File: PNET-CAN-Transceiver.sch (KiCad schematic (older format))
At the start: 15 parts

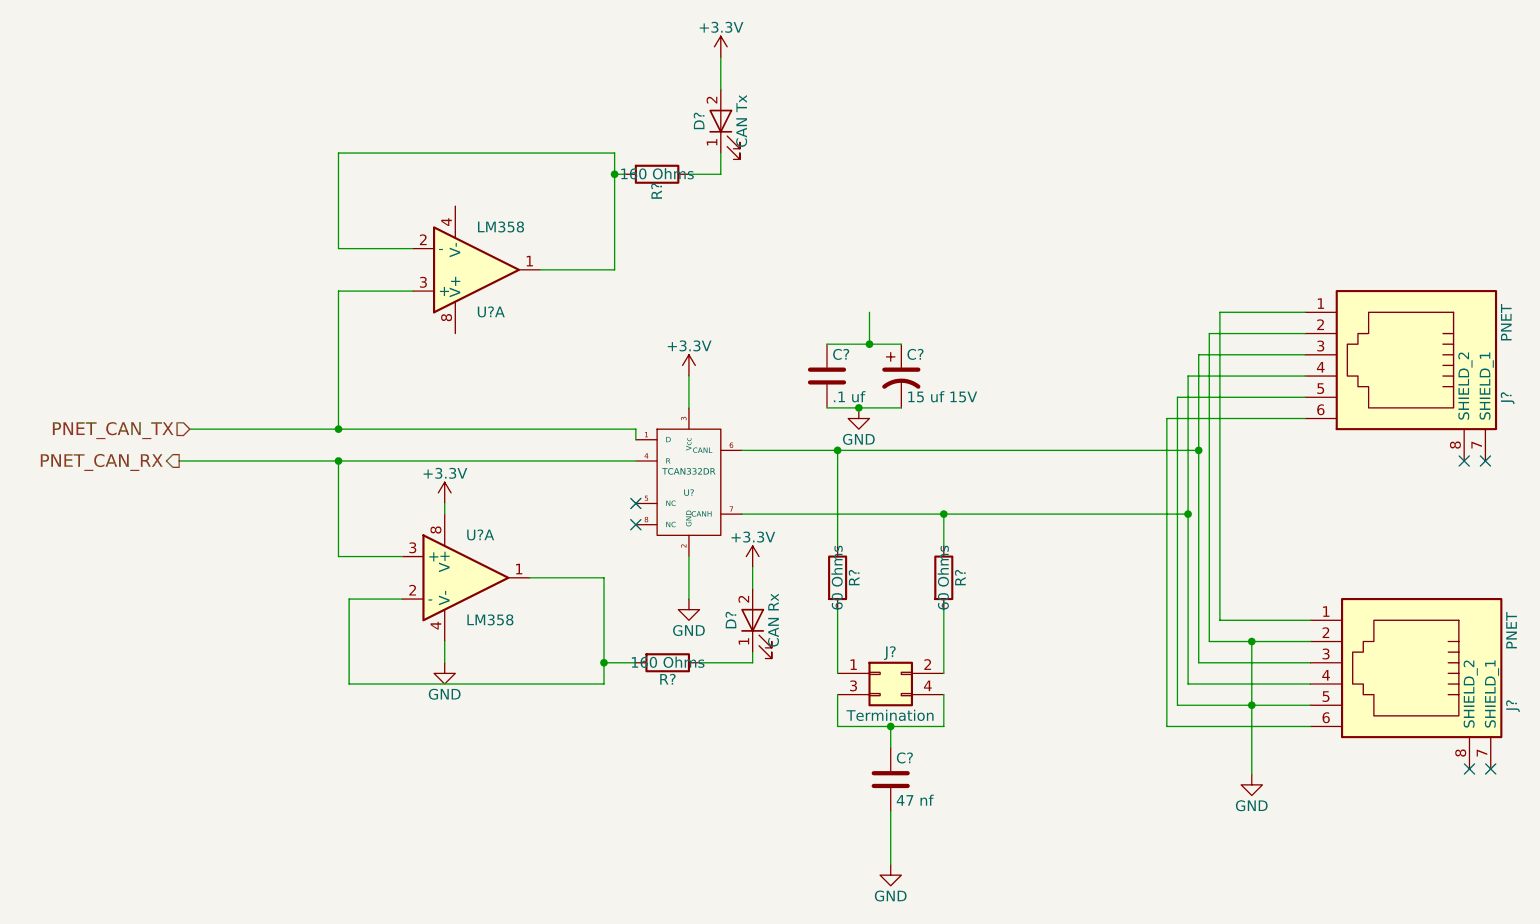
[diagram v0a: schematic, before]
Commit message: Start on LCC <=> PNET router.
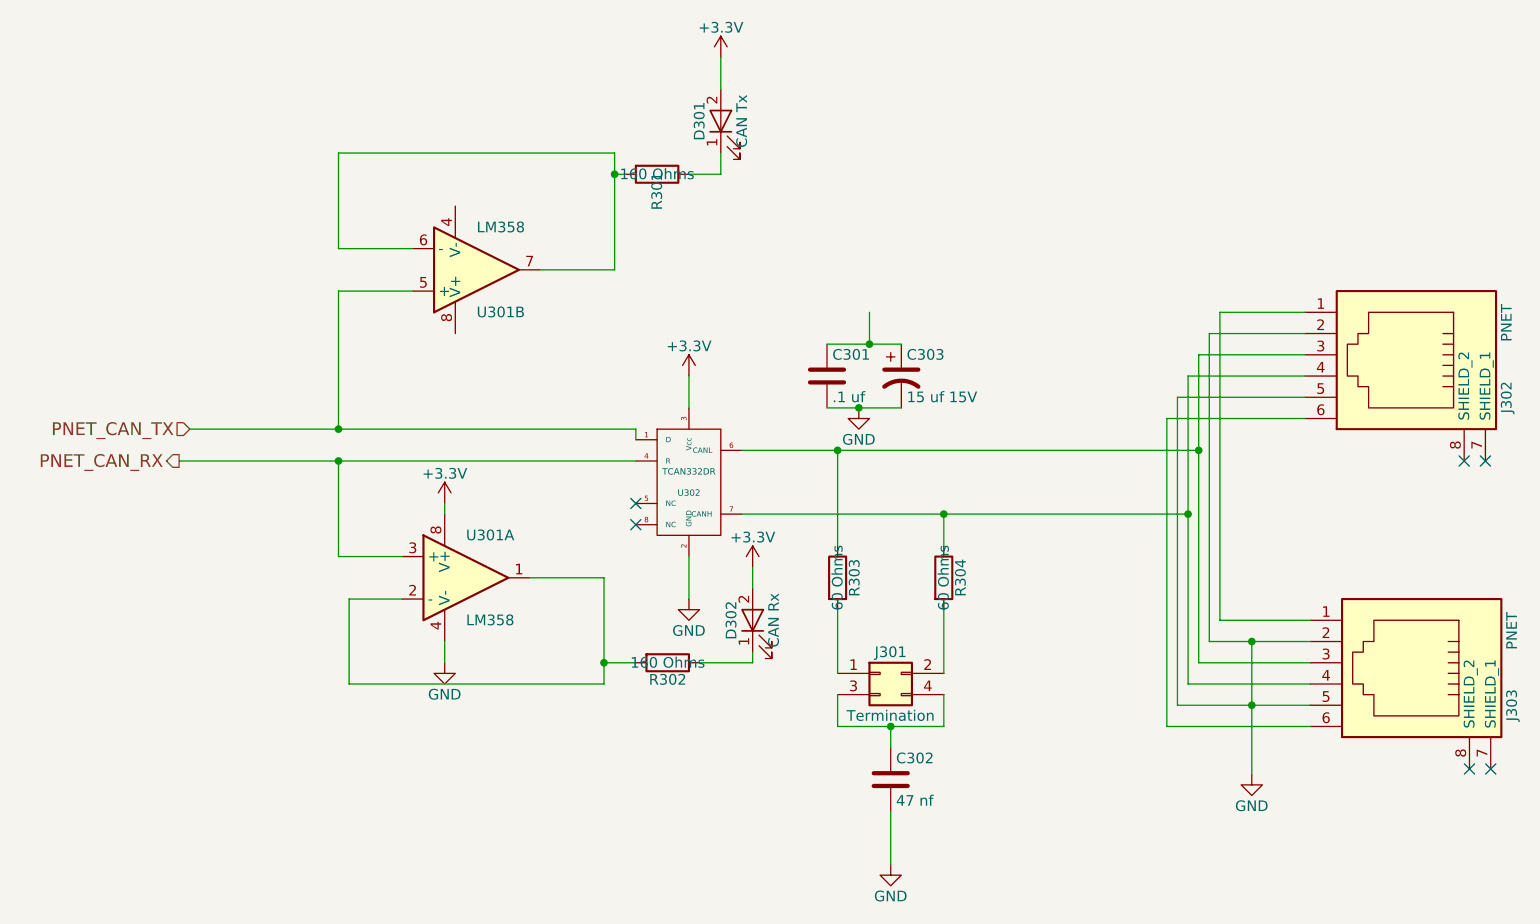
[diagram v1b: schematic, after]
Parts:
- gave numbers to parts that had none: 14
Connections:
- net PNET_CAN_TX: now also U301.5 (+); no longer U301.3 (+)
- new net: R301.2, U301.6 (-), U301.7
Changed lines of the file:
@@
 $EndDescr
 $Comp
-L TCAN332DR U?
+L TCAN332DR U302
 U 1 1 63C03DBA
 P 4600 2950
-F 0 "U?" H 4600 2900 30  0000 C CNN
+F 0 "U302" H 4600 2900 30  0000 C CNN
 F 1 "TCAN332DR" H 4600 3000 30  0000 C CNN
 F 2 "Housings_SOIC:SOIC-8-1EP_3.9x4.9mm_Pitch1.27mm" H 4600 2950 60  0001 C CNN
@@
 NoConn ~ 4350 3150
 $Comp
-L +3.3V #PWR?
+L +3.3V #PWR019
 U 1 1 63C03DBD
 P 4600 2450
-F 0 "#PWR?" H 4600 2300 50  0001 C CNN
+F 0 "#PWR019" H 4600 2300 50  0001 C CNN
 F 1 "+3.3V" H 4600 2590 50  0000 C CNN
 F 2 "" H 4600 2450 50  0001 C CNN
@@
 $EndComp
 $Comp
-L GND #PWR?
+L GND #PWR020
 U 1 1 63C03DBE
 P 4600 3500
-F 0 "#PWR?" H 4600 3250 50  0001 C CNN
+F 0 "#PWR020" H 4600 3250 50  0001 C CNN
 F 1 "GND" H 4600 3350 50  0000 C CNN
 F 2 "" H 4600 3500 50  0001 C CNN
@@
 $EndComp
 $Comp
-L C C?
+L C C301
 U 1 1 63C03DC0
 P 5250 2450
-F 0 "C?" H 5275 2550 50  0000 L CNN
+F 0 "C301" H 5275 2550 50  0000 L CNN
 F 1 ".1 uf" H 5275 2350 50  0000 L CNN
 F 2 "Capacitors_THT:C_Rect_L4.0mm_W2.5mm_P2.50mm" H 5288 2300 50  0001 C CNN
@@
 $EndComp
 $Comp
-L CP1 C?
+L CP1 C303
 U 1 1 63C03DC1
 P 5600 2450
-F 0 "C?" H 5625 2550 50  0000 L CNN
+F 0 "C303" H 5625 2550 50  0000 L CNN
 F 1 "15 uf 15V" H 5625 2350 50  0000 L CNN
 F 2 "Capacitors_THT:CP_Radial_D6.3mm_P2.50mm" H 5600 2450 50  0001 C CNN
@@
 $EndComp
 $Comp
-L Conn_02x02_Odd_Even J?
+L Conn_02x02_Odd_Even J301
 U 1 1 63C03DC2
 P 5500 3850
-F 0 "J?" H 5550 3950 50  0000 C CNN
+F 0 "J301" H 5550 3950 50  0000 C CNN
 F 1 "Termination" H 5550 3650 50  0000 C CNN
 F 2 "Pin_Headers:Pin_Header_Straight_2x02_Pitch2.54mm" H 5500 3850 50  0001 C CNN
@@
 $EndComp
 $Comp
-L R R?
+L R R303
 U 1 1 63C03DC3
 P 5300 3400
-F 0 "R?" V 5380 3400 50  0000 C CNN
+F 0 "R303" V 5380 3400 50  0000 C CNN
 F 1 "60 Ohms" V 5300 3400 50  0000 C CNN
 F 2 "Resistors_THT:R_Axial_DIN0204_L3.6mm_D1.6mm_P2.54mm_Vertical" V 5230 3400 50  0001 C CNN
@@
 $EndComp
 $Comp
-L R R?
+L R R304
 U 1 1 63C03DC4
 P 5800 3400
-F 0 "R?" V 5880 3400 50  0000 C CNN
+F 0 "R304" V 5880 3400 50  0000 C CNN
 F 1 "60 Ohms" V 5800 3400 50  0000 C CNN
 F 2 "Resistors_THT:R_Axial_DIN0204_L3.6mm_D1.6mm_P2.54mm_Vertical" V 5730 3400 50  0001 C CNN
@@
 $EndComp
 $Comp
-L C C?
+L C C302
 U 1 1 63C03DC5
 P 5550 4350
-F 0 "C?" H 5575 4450 50  0000 L CNN
+F 0 "C302" H 5575 4450 50  0000 L CNN
 F 1 "47 nf" H 5575 4250 50  0000 L CNN
 F 2 "Capacitors_THT:C_Rect_L4.0mm_W2.5mm_P2.50mm" H 5588 4200 50  0001 C CNN
@@
 $EndComp
 $Comp
-L GND #PWR?
+L GND #PWR021
 U 1 1 63C03DC6
 P 5550 4750
-F 0 "#PWR?" H 5550 4500 50  0001 C CNN
+F 0 "#PWR021" H 5550 4500 50  0001 C CNN
 F 1 "GND" H 5550 4600 50  0000 C CNN
 F 2 "" H 5550 4750 50  0001 C CNN
@@
 $EndComp
 $Comp
-L GND #PWR?
+L GND #PWR022
 U 1 1 63C03DC8
 P 5400 2600
-F 0 "#PWR?" H 5400 2350 50  0001 C CNN
+F 0 "#PWR022" H 5400 2350 50  0001 C CNN
 F 1 "GND" H 5400 2450 50  0000 C CNN
 F 2 "" H 5400 2600 50  0001 C CNN
@@
 PNET_CAN_RX
 $Comp
-L LM358 U?
-U 1 1 63C03DCE
+L LM358 U301
+U 2 1 63C03DCE
 P 3600 1950
-F 0 "U?" H 3600 2150 50  0000 L CNN
+F 0 "U301" H 3600 2150 50  0000 L CNN
 F 1 "LM358" H 3600 1750 50  0000 L CNN
 F 2 "Housings_DIP:DIP-8_W7.62mm" H 3600 1950 50  0001 C CNN
 F 3 "" H 3600 1950 50  0001 C CNN
 F 4 "595-LM358AP" H 3600 1950 60  0001 C CNN "Mouser Part Number"
-	1    3600 1950
+	2    3600 1950
 	1    0    0    1
 $EndComp
 $Comp
-L LM358 U?
+L LM358 U301
 U 1 1 63C03DCF
 P 3550 3400
-F 0 "U?" H 3550 3600 50  0000 L CNN
+F 0 "U301" H 3550 3600 50  0000 L CNN
 F 1 "LM358" H 3550 3200 50  0000 L CNN
 F 2 "Housings_DIP:DIP-8_W7.62mm" H 3550 3400 50  0001 C CNN
@@
 $EndComp
 $Comp
-L GND #PWR?
+L GND #PWR023
 U 1 1 63C03DD0
 P 3450 3800
-F 0 "#PWR?" H 3450 3550 50  0001 C CNN
+F 0 "#PWR023" H 3450 3550 50  0001 C CNN
 F 1 "GND" H 3450 3650 50  0000 C CNN
 F 2 "" H 3450 3800 50  0001 C CNN
@@
 $EndComp
 $Comp
-L +3.3V #PWR?
+L +3.3V #PWR024
 U 1 1 63C03DD1
 P 3450 3050
-F 0 "#PWR?" H 3450 2900 50  0001 C CNN
+F 0 "#PWR024" H 3450 2900 50  0001 C CNN
 F 1 "+3.3V" H 3450 3190 50  0000 C CNN
 F 2 "" H 3450 3050 50  0001 C CNN
@@
 $EndComp
 $Comp
-L R R?
+L R R301
 U 1 1 63C03DD2
 P 4450 1500
-F 0 "R?" H 4530 1500 50  0000 C CNN
+F 0 "R301" H 4530 1500 50  0000 C CNN
 F 1 "160 Ohms" V 4450 1500 50  0000 C CNN
 F 2 "Resistors_THT:R_Axial_DIN0204_L3.6mm_D1.6mm_P1.90mm_Vertical" V 4380 1500 50  0001 C CNN
@@
 $EndComp
 $Comp
-L R R?
+L R R302
 U 1 1 63C03DD3
 P 4500 3800
-F 0 "R?" V 4580 3800 50  0000 C CNN
+F 0 "R302" V 4580 3800 50  0000 C CNN
 F 1 "160 Ohms" V 4500 3800 50  0000 C CNN
 F 2 "Resistors_THT:R_Axial_DIN0204_L3.6mm_D1.6mm_P1.90mm_Vertical" V 4430 3800 50  0001 C CNN
@@
 $EndComp
 $Comp
-L LED D?
+L LED D301
 U 1 1 63C03DD4
 P 4750 1250
-F 0 "D?" H 4750 1350 50  0000 C CNN
+F 0 "D301" H 4750 1350 50  0000 C CNN
 F 1 "CAN Tx" H 4750 1150 50  0000 C CNN
 F 2 "LEDs:LED_D3.0mm" H 4750 1250 50  0001 C CNN
@@
 $EndComp
 $Comp
-L LED D?
+L LED D302
 U 1 1 63C03DD5
 P 4900 3600
-F 0 "D?" H 4900 3700 50  0000 C CNN
+F 0 "D302" H 4900 3700 50  0000 C CNN
 F 1 "CAN Rx" H 4900 3500 50  0000 C CNN
 F 2 "LEDs:LED_D3.0mm" H 4900 3600 50  0001 C CNN
@@
 $EndComp
 $Comp
-L +3.3V #PWR?
+L +3.3V #PWR025
 U 1 1 63C03DD6
 P 4750 950
-F 0 "#PWR?" H 4750 800 50  0001 C CNN
+F 0 "#PWR025" H 4750 800 50  0001 C CNN
 F 1 "+3.3V" H 4750 1090 50  0000 C CNN
 F 2 "" H 4750 950 50  0001 C CNN
@@
 $EndComp
 $Comp
-L +3.3V #PWR?
+L +3.3V #PWR026
 U 1 1 63C03DD7
 P 4900 3350
-F 0 "#PWR?" H 4900 3200 50  0001 C CNN
+F 0 "#PWR026" H 4900 3200 50  0001 C CNN
 F 1 "+3.3V" H 4900 3490 50  0000 C CNN
 F 2 "" H 4900 3350 50  0001 C CNN
@@
 $EndComp
 $Comp
-L RJ12 J?
+L RJ12 J302
 U 1 1 63C04A35
 P 7950 2350
-F 0 "J?" H 8150 2850 50  0000 C CNN
+F 0 "J302" H 8150 2850 50  0000 C CNN
 F 1 "PNET" H 7800 2850 50  0000 C CNN
 F 2 "Connectors:RJ12_E" H 7950 2350 50  0001 C CNN
@@
 $EndComp
 $Comp
-L RJ12 J?
+L RJ12 J303
 U 1 1 63C04C52
 P 7975 3800
-F 0 "J?" H 8175 4300 50  0000 C CNN
+F 0 "J303" H 8175 4300 50  0000 C CNN
 F 1 "PNET" H 7825 4300 50  0000 C CNN
 F 2 "Connectors:RJ12_E" H 7975 3800 50  0001 C CNN
@@
 $EndComp
 $Comp
-L GND #PWR?
+L GND #PWR027
 U 1 1 63C05BB2
 P 7250 4325
-F 0 "#PWR?" H 7250 4075 50  0001 C CNN
+F 0 "#PWR027" H 7250 4075 50  0001 C CNN
 F 1 "GND" H 7250 4175 50  0000 C CNN
 F 2 "" H 7250 4325 50  0001 C CNN

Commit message: Completed initial HW design.
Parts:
- C301: footprint Capacitors_THT:C_Rect_L4.0mm_W2.5mm_P2.50mm -> Capacitors_SMD:C_0603; Mouser Part Number 594-K104Z15Y5VF5TL2 -> 603-CC603KPX7R9BB104
- C302: footprint Capacitors_THT:C_Rect_L4.0mm_W2.5mm_P2.50mm -> Capacitors_SMD:C_0603; Mouser Part Number 594-K473K15X7RF5TL2 -> 963-GMK107BJ473KAHT
- C303: footprint Capacitors_THT:CP_Radial_D6.3mm_P2.50mm -> Capacitors_SMD:CP_Elec_4x5.8; Mouser Part Number 710-860080773002 -> 647-UUD1C150MCL
- D301: value CAN Tx -> PNET Tx; footprint LEDs:LED_D3.0mm -> LEDs:LED_0603; Mouser Part Number 710-151031SS04000 -> 710-150060SS75000
- D302: value CAN Rx -> PNET Rx; footprint LEDs:LED_D3.0mm -> LEDs:LED_0603; Mouser Part Number 710-151033YS03000 -> 710-150060YS75000
- R301, R302: footprint Resistors_THT:R_Axial_DIN0204_L3.6mm_D1.6mm_P1.90mm_Vertical -> Resistors_SMD:R_0603; Mouser Part Number 603-CFR-25JB-52-160R -> 603-AC0603JR-07160RL
- R303, R304: footprint Resistors_THT:R_Axial_DIN0204_L3.6mm_D1.6mm_P2.54mm_Vertical -> Resistors_SMD:R_1206; Mouser Part Number 603-RSF2WSJT-52-60R -> 71-CRCW120660R0KNAIF
- U301: footprint Housings_DIP:DIP-8_W7.62mm -> Housings_SOIC:SOIC-8_3.9x4.9mm_Pitch1.27mm; Mouser Part Number 595-LM358AP -> 595-LM358DR
- U302: footprint Housings_SOIC:SOIC-8-1EP_3.9x4.9mm_Pitch1.27mm -> Housings_SOIC:SOIC-8_3.9x4.9mm_Pitch1.27mm
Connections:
- net +3V3: now also C301.1, C303.1
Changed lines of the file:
@@
 LIBS:lm2574n-5
 LIBS:sn65hvd233-ht
+LIBS:ap63205
 LIBS:LCC-PNET-Router-cache
 EELAYER 25 0
@@
 F 0 "U302" H 4600 2900 30  0000 C CNN
 F 1 "TCAN332DR" H 4600 3000 30  0000 C CNN
-F 2 "Housings_SOIC:SOIC-8-1EP_3.9x4.9mm_Pitch1.27mm" H 4600 2950 60  0001 C CNN
+F 2 "Housings_SOIC:SOIC-8_3.9x4.9mm_Pitch1.27mm" H 4600 2950 60  0001 C CNN
 F 3 "" H 4600 2950 60  0000 C CNN
 F 4 "595-TCAN332DR" H 4600 2950 60  0001 C CNN "Mouser Part Number"
@@
 NoConn ~ 4350 3150
 $Comp
-L +3.3V #PWR019
+L +3.3V #PWR303
 U 1 1 63C03DBD
 P 4600 2450
-F 0 "#PWR019" H 4600 2300 50  0001 C CNN
+F 0 "#PWR303" H 4600 2300 50  0001 C CNN
 F 1 "+3.3V" H 4600 2590 50  0000 C CNN
 F 2 "" H 4600 2450 50  0001 C CNN
@@
 $EndComp
 $Comp
-L GND #PWR020
+L GND #PWR304
 U 1 1 63C03DBE
 P 4600 3500
-F 0 "#PWR020" H 4600 3250 50  0001 C CNN
+F 0 "#PWR304" H 4600 3250 50  0001 C CNN
 F 1 "GND" H 4600 3350 50  0000 C CNN
 F 2 "" H 4600 3500 50  0001 C CNN
@@
 F 0 "C301" H 5275 2550 50  0000 L CNN
 F 1 ".1 uf" H 5275 2350 50  0000 L CNN
-F 2 "Capacitors_THT:C_Rect_L4.0mm_W2.5mm_P2.50mm" H 5288 2300 50  0001 C CNN
+F 2 "Capacitors_SMD:C_0603" H 5288 2300 50  0001 C CNN
 F 3 "" H 5250 2450 50  0001 C CNN
-F 4 "594-K104Z15Y5VF5TL2" H 5250 2450 60  0001 C CNN "Mouser Part Number"
+F 4 "603-CC603KPX7R9BB104" H 5250 2450 60  0001 C CNN "Mouser Part Number"
 	1    5250 2450
 	1    0    0    -1
@@
 F 0 "C303" H 5625 2550 50  0000 L CNN
 F 1 "15 uf 15V" H 5625 2350 50  0000 L CNN
-F 2 "Capacitors_THT:CP_Radial_D6.3mm_P2.50mm" H 5600 2450 50  0001 C CNN
+F 2 "Capacitors_SMD:CP_Elec_4x5.8" H 5600 2450 50  0001 C CNN
 F 3 "" H 5600 2450 50  0001 C CNN
-F 4 "710-860080773002" H 5600 2450 60  0001 C CNN "Mouser Part Number"
+F 4 "647-UUD1C150MCL" H 5600 2450 60  0001 C CNN "Mouser Part Number"
 	1    5600 2450
 	1    0    0    -1
@@
 F 0 "R303" V 5380 3400 50  0000 C CNN
 F 1 "60 Ohms" V 5300 3400 50  0000 C CNN
-F 2 "Resistors_THT:R_Axial_DIN0204_L3.6mm_D1.6mm_P2.54mm_Vertical" V 5230 3400 50  0001 C CNN
+F 2 "Resistors_SMD:R_1206" V 5230 3400 50  0001 C CNN
 F 3 "" H 5300 3400 50  0001 C CNN
-F 4 "603-RSF2WSJT-52-60R" V 5300 3400 60  0001 C CNN "Mouser Part Number"
+F 4 "71-CRCW120660R0KNAIF" V 5300 3400 60  0001 C CNN "Mouser Part Number"
 	1    5300 3400
 	1    0    0    -1
@@
 F 0 "R304" V 5880 3400 50  0000 C CNN
 F 1 "60 Ohms" V 5800 3400 50  0000 C CNN
-F 2 "Resistors_THT:R_Axial_DIN0204_L3.6mm_D1.6mm_P2.54mm_Vertical" V 5730 3400 50  0001 C CNN
+F 2 "Resistors_SMD:R_1206" V 5730 3400 50  0001 C CNN
 F 3 "" H 5800 3400 50  0001 C CNN
-F 4 "603-RSF2WSJT-52-60R" V 5800 3400 60  0001 C CNN "Mouser Part Number"
+F 4 "71-CRCW120660R0KNAIF" V 5800 3400 60  0001 C CNN "Mouser Part Number"
 	1    5800 3400
 	1    0    0    -1
@@
 F 0 "C302" H 5575 4450 50  0000 L CNN
 F 1 "47 nf" H 5575 4250 50  0000 L CNN
-F 2 "Capacitors_THT:C_Rect_L4.0mm_W2.5mm_P2.50mm" H 5588 4200 50  0001 C CNN
+F 2 "Capacitors_SMD:C_0603" H 5588 4200 50  0001 C CNN
 F 3 "" H 5550 4350 50  0001 C CNN
-F 4 "594-K473K15X7RF5TL2" H 5550 4350 60  0001 C CNN "Mouser Part Number"
+F 4 "963-GMK107BJ473KAHT" H 5550 4350 60  0001 C CNN "Mouser Part Number"
 	1    5550 4350
 	1    0    0    -1
 $EndComp
 $Comp
-L GND #PWR021
+L GND #PWR309
 U 1 1 63C03DC6
 P 5550 4750
-F 0 "#PWR021" H 5550 4500 50  0001 C CNN
+F 0 "#PWR309" H 5550 4500 50  0001 C CNN
 F 1 "GND" H 5550 4600 50  0000 C CNN
 F 2 "" H 5550 4750 50  0001 C CNN
@@
 $EndComp
 $Comp
-L GND #PWR022
+L GND #PWR307
 U 1 1 63C03DC8
 P 5400 2600
-F 0 "#PWR022" H 5400 2350 50  0001 C CNN
+F 0 "#PWR307" H 5400 2350 50  0001 C CNN
 F 1 "GND" H 5400 2450 50  0000 C CNN
 F 2 "" H 5400 2600 50  0001 C CNN
@@
 F 0 "U301" H 3600 2150 50  0000 L CNN
 F 1 "LM358" H 3600 1750 50  0000 L CNN
-F 2 "Housings_DIP:DIP-8_W7.62mm" H 3600 1950 50  0001 C CNN
+F 2 "Housings_SOIC:SOIC-8_3.9x4.9mm_Pitch1.27mm" H 3600 1950 50  0001 C CNN
 F 3 "" H 3600 1950 50  0001 C CNN
-F 4 "595-LM358AP" H 3600 1950 60  0001 C CNN "Mouser Part Number"
+F 4 "595-LM358DR" H 3600 1950 60  0001 C CNN "Mouser Part Number"
 	2    3600 1950
 	1    0    0    1
@@
 F 0 "U301" H 3550 3600 50  0000 L CNN
 F 1 "LM358" H 3550 3200 50  0000 L CNN
-F 2 "Housings_DIP:DIP-8_W7.62mm" H 3550 3400 50  0001 C CNN
+F 2 "Housings_SOIC:SOIC-8_3.9x4.9mm_Pitch1.27mm" H 3550 3400 50  0001 C CNN
 F 3 "" H 3550 3400 50  0001 C CNN
-F 4 "595-LM358AP" H 3550 3400 60  0001 C CNN "Mouser Part Number"
+F 4 "595-LM358DR" H 3550 3400 60  0001 C CNN "Mouser Part Number"
 	1    3550 3400
 	1    0    0    -1
 $EndComp
 $Comp
-L GND #PWR023
+L GND #PWR302
 U 1 1 63C03DD0
 P 3450 3800
-F 0 "#PWR023" H 3450 3550 50  0001 C CNN
+F 0 "#PWR302" H 3450 3550 50  0001 C CNN
 F 1 "GND" H 3450 3650 50  0000 C CNN
 F 2 "" H 3450 3800 50  0001 C CNN
@@
 $EndComp
 $Comp
-L +3.3V #PWR024
+L +3.3V #PWR301
 U 1 1 63C03DD1
 P 3450 3050
-F 0 "#PWR024" H 3450 2900 50  0001 C CNN
+F 0 "#PWR301" H 3450 2900 50  0001 C CNN
 F 1 "+3.3V" H 3450 3190 50  0000 C CNN
 F 2 "" H 3450 3050 50  0001 C CNN
@@
 F 0 "R301" H 4530 1500 50  0000 C CNN
 F 1 "160 Ohms" V 4450 1500 50  0000 C CNN
-F 2 "Resistors_THT:R_Axial_DIN0204_L3.6mm_D1.6mm_P1.90mm_Vertical" V 4380 1500 50  0001 C CNN
+F 2 "Resistors_SMD:R_0603" V 4380 1500 50  0001 C CNN
 F 3 "" H 4450 1500 50  0001 C CNN
-F 4 "603-CFR-25JB-52-160R" H 4450 1500 60  0001 C CNN "Mouser Part Number"
+F 4 "603-AC0603JR-07160RL" H 4450 1500 60  0001 C CNN "Mouser Part Number"
 	1    4450 1500
 	0    1    1    0
@@
 F 0 "R302" V 4580 3800 50  0000 C CNN
 F 1 "160 Ohms" V 4500 3800 50  0000 C CNN
-F 2 "Resistors_THT:R_Axial_DIN0204_L3.6mm_D1.6mm_P1.90mm_Vertical" V 4430 3800 50  0001 C CNN
+F 2 "Resistors_SMD:R_0603" V 4430 3800 50  0001 C CNN
 F 3 "" H 4500 3800 50  0001 C CNN
-F 4 "603-CFR-25JB-52-160R" V 4500 3800 60  0001 C CNN "Mouser Part Number"
+F 4 "603-AC0603JR-07160RL" V 4500 3800 60  0001 C CNN "Mouser Part Number"
 	1    4500 3800
 	0    1    1    0
@@
 P 4750 1250
 F 0 "D301" H 4750 1350 50  0000 C CNN
-F 1 "CAN Tx" H 4750 1150 50  0000 C CNN
-F 2 "LEDs:LED_D3.0mm" H 4750 1250 50  0001 C CNN
+F 1 "PNET Tx" H 4750 1150 50  0000 C CNN
+F 2 "LEDs:LED_0603" H 4750 1250 50  0001 C CNN
 F 3 "" H 4750 1250 50  0001 C CNN
-F 4 "710-151031SS04000" H 4750 1250 60  0001 C CNN "Mouser Part Number"
+F 4 "710-150060SS75000" H 4750 1250 60  0001 C CNN "Mouser Part Number"
 	1    4750 1250
 	0    -1   -1   0
@@
 P 4900 3600
 F 0 "D302" H 4900 3700 50  0000 C CNN
-F 1 "CAN Rx" H 4900 3500 50  0000 C CNN
-F 2 "LEDs:LED_D3.0mm" H 4900 3600 50  0001 C CNN
+F 1 "PNET Rx" H 4900 3500 50  0000 C CNN
+F 2 "LEDs:LED_0603" H 4900 3600 50  0001 C CNN
 F 3 "" H 4900 3600 50  0001 C CNN
-F 4 "710-151033YS03000" H 4900 3600 60  0001 C CNN "Mouser Part Number"
+F 4 "710-150060YS75000" H 4900 3600 60  0001 C CNN "Mouser Part Number"
 	1    4900 3600
 	0    -1   -1   0
 $EndComp
 $Comp
-L +3.3V #PWR025
+L +3.3V #PWR305
 U 1 1 63C03DD6
 P 4750 950
-F 0 "#PWR025" H 4750 800 50  0001 C CNN
+F 0 "#PWR305" H 4750 800 50  0001 C CNN
 F 1 "+3.3V" H 4750 1090 50  0000 C CNN
 F 2 "" H 4750 950 50  0001 C CNN
@@
 $EndComp
 $Comp
-L +3.3V #PWR026
+L +3.3V #PWR306
 U 1 1 63C03DD7
 P 4900 3350
-F 0 "#PWR026" H 4900 3200 50  0001 C CNN
+F 0 "#PWR306" H 4900 3200 50  0001 C CNN
 F 1 "+3.3V" H 4900 3490 50  0000 C CNN
 F 2 "" H 4900 3350 50  0001 C CNN
@@
 $EndComp
 $Comp
-L GND #PWR027
+L GND #PWR310
 U 1 1 63C05BB2
 P 7250 4325
-F 0 "#PWR027" H 7250 4075 50  0001 C CNN
+F 0 "#PWR310" H 7250 4075 50  0001 C CNN
 F 1 "GND" H 7250 4175 50  0000 C CNN
 F 2 "" H 7250 4325 50  0001 C CNN
@@
 NoConn ~ 8275 4300
 NoConn ~ 8375 4300
+$Comp
+L +3.3V #PWR308
+U 1 1 6411F0A8
+P 5450 2150
+F 0 "#PWR308" H 5450 2000 50  0001 C CNN
+F 1 "+3.3V" H 5450 2290 50  0000 C CNN
+F 2 "" H 5450 2150 50  0001 C CNN
+F 3 "" H 5450 2150 50  0001 C CNN
+	1    5450 2150
+	1    0    0    -1
+$EndComp
 $EndSCHEMATC
